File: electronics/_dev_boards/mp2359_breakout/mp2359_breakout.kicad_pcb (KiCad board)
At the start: 2 copper layers, 30 x 30 mm, 12 parts, among them J1 CONN_01X03, J2 CONN_01X02, P1 SYMBOL, U1 MP2359

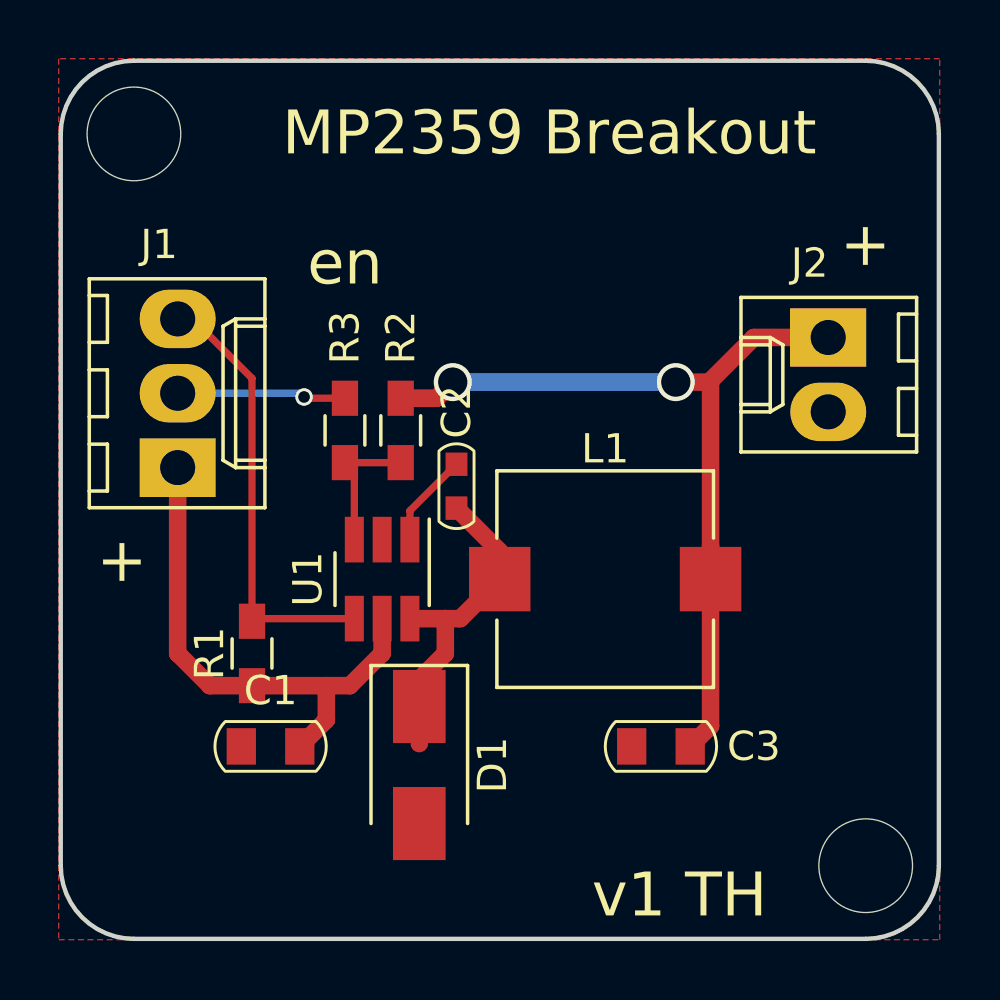
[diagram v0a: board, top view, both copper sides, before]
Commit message: mp2359_breakout: properly connect ground
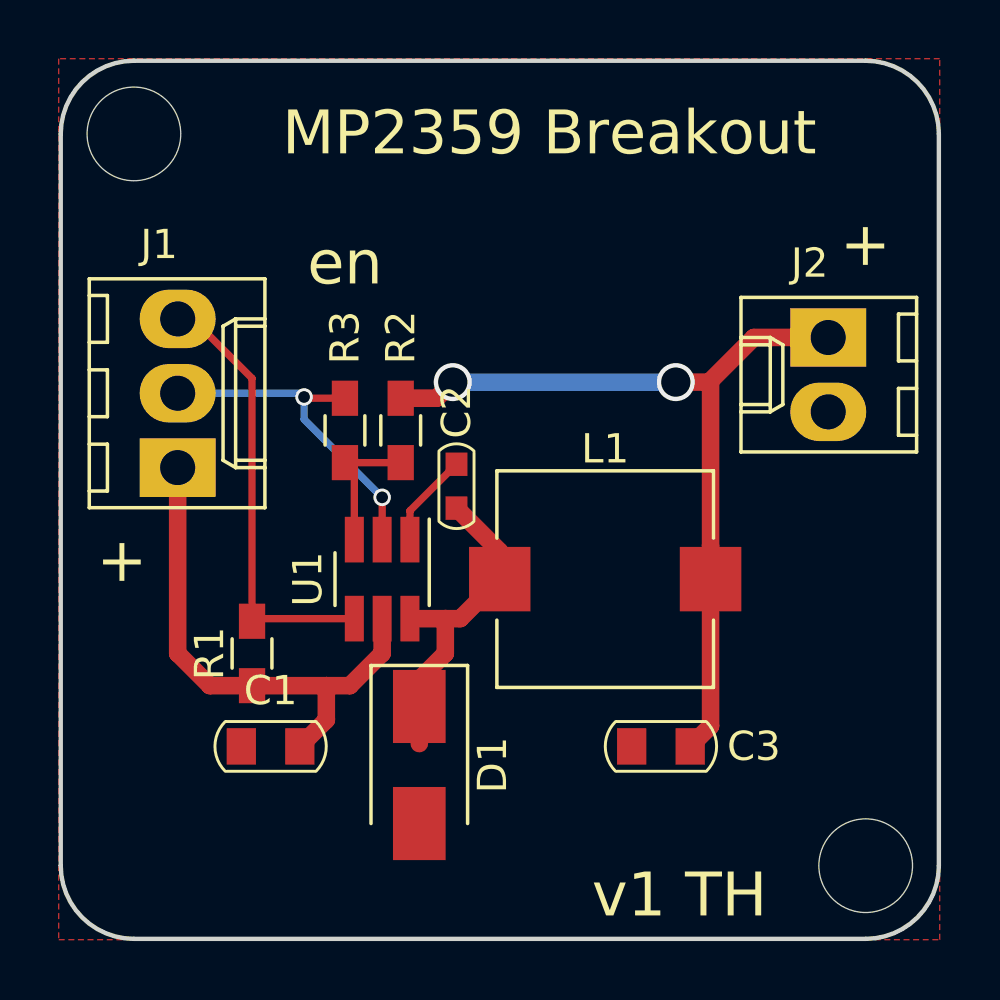
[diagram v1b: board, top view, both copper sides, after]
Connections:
- U1 pad 2: (no net) -> GND
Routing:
- net GND: track 6.03 -> 12.0 mm, vias 1 -> 2
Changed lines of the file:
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@@
 (kicad_pcb (version 4) (host pcbnew 4.0.6-e0-6349~53~ubuntu14.04.1)
   (general
-    (links 19)
+    (links 20)
     (no_connects 0)
-    (area 155.575 68.58 186.300001 100.830001)
+    (area 0 0 0 0)
     (thickness 1.6)
     (drawings 5)
-    (tracks 49)
+    (tracks 53)
     (zones 0)
     (modules 12)
@@
     (pad 1 smd rect (at -1.35 -0.95 270) (size 1.56 0.65) (layers F.Cu F.Paste F.Mask)
       (net 2 "Net-(C2-Pad1)"))
-    (pad 2 smd rect (at -1.35 0 270) (size 1.56 0.65) (layers F.Cu F.Paste F.Mask))
+    (pad 2 smd rect (at -1.35 0 270) (size 1.56 0.65) (layers F.Cu F.Paste F.Mask)
+      (net 1 GND))
     (pad 3 smd rect (at -1.35 0.95 270) (size 1.56 0.65) (layers F.Cu F.Paste F.Mask)
       (net 4 "Net-(R2-Pad2)"))
@@
     (effects (font (size 1.5 1.5) (thickness 0.3)))
   )
+  (segment (start 167.005 86.915) (end 167.005 85.471) (width 0.25) (layer F.Cu) (net 1) (status 400000))
+  (segment (start 164.338 82.804) (end 164.338 82.042) (width 0.25) (layer B.Cu) (net 1))
+  (segment (start 167.005 85.471) (end 164.338 82.804) (width 0.25) (layer B.Cu) (net 1))
+  (via (at 167.005 85.471) (size 0.6) (drill 0.4) (layers F.Cu B.Cu) (net 1))
   (segment (start 160.02 81.915) (end 164.211 81.915) (width 0.25) (layer B.Cu) (net 1))
   (segment (start 164.381 82.085) (end 165.735 82.085) (width 0.25) (layer F.Cu) (net 1))
